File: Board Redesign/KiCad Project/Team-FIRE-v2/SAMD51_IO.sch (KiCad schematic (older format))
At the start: 20 parts, among them SW1 RESET, U5 SAMD51, U6 AT25DF041x-UxN-x, Y1 32.768kHz

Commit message: Fixed some stuff (woops)
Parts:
- R15: footprint Resistor_SMD:R_0603_1608Metric -> (none); Link https://www.mouser.com/ProductDetail/Vishay-Beyschlag/MCT06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 -> (none); MPN MCT06030E1002BP100 -> (none); Manufacturer Vishay -> (none); Supplier Mouser -> (none); Supplier PN 594-MCT06030E1002BP1 -> (none); Tolerance 0.1% -> (none); Type Thin Film Resistor -> (none); Voltage Rating 75 V -> (none)
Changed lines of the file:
@@
 Comment4 ""
 $EndDescr
+Text GLabel 1260 3190 0    50   Input ~ 0
+USB_D-
+Text GLabel 1260 3290 0    50   Input ~ 0
+USB_D+
+Text GLabel 1260 2790 0    50   Input ~ 0
+SDA
+Text GLabel 1260 2890 0    50   Input ~ 0
+SCL
 $Comp
 L Team-FIRE:SAMD51 U?
@@
 	1    0    0    -1
 $EndComp
+Text GLabel 1260 3490 0    50   Input ~ 0
+SWCLK
+Text GLabel 1260 3590 0    50   Input ~ 0
+SWDIO
 Text GLabel 3980 1130 0    50   Input ~ 0
 RX_LED
+Text GLabel 1260 3390 0    50   Input ~ 0
+TX_LED
 Text GLabel 6740 3010 0    50   Input ~ 0
 SWO
@@
 Text Notes 6190 4060 0    50   ~ 10
 SAMD51 Power decoupling capacitors
-Text GLabel 3050 4800 2    50   Input ~ 0
+$Comp
+L Memory_Flash:AT25DF041x-UxN-x U?
+U 1 1 5F15C396
+P 2620 4970
+AR Path="/5E4F8378/5EA71818/5F15C396" Ref="U?"  Part="1"
+AR Path="/5E4F8378/5ED4DEFC/5ED7D75E/5F15C396" Ref="U?"  Part="1"
+AR Path="/5E4F8378/5ED4DEFC/5F15C396" Ref="U6"  Part="1"
+F 0 "U6" H 2770 4550 50  0000 L CNN
+F 1 "AT25DF041x-UxN-x" H 2770 4450 50  0000 L CNN
+F 2 "Package_CSP:WLCSP-8_1.58x1.63x0.35mm_Layout3x5_P0.35x0.4mm_Ball0.25mm_Pad0.25mm_NSMD" H 2420 4370 50  0001 C CNN
+F 3 "http://www.adestotech.com/wp-content/uploads/DS-AT25DF041B_040.pdf" H 2620 5670 50  0001 C CNN
+	1    2620 4970
+	1    0    0    -1
+$EndComp
+Text GLabel 3220 4770 2    50   Input ~ 0
 FLASH_MISO
+Text GLabel 2020 4870 0    50   Input ~ 0
+FLASH_SCK
+Text GLabel 2020 4770 0    50   Input ~ 0
+FLASH_MOSI
+Wire Wire Line
+	2620 5490 2620 5470
 $Comp
 L power:+3.3V #PWR?
 U 1 1 5F15C3A7
-P 2350 4300
+P 2620 4380
 AR Path="/5E4F8378/5EA71818/5F15C3A7" Ref="#PWR?"  Part="1"
 AR Path="/5E4F8378/5ED4DEFC/5ED7D75E/5F15C3A7" Ref="#PWR?"  Part="1"
 AR Path="/5E4F8378/5ED4DEFC/5F15C3A7" Ref="#PWR0138"  Part="1"
-F 0 "#PWR0138" H 2350 4150 50  0001 C CNN
-F 1 "+3.3V" H 2365 4473 50  0000 C CNN
-F 2 "" H 2350 4300 50  0001 C CNN
-F 3 "" H 2350 4300 50  0001 C CNN
-	1    2350 4300
-	1    0    0    -1
-$EndComp
+F 0 "#PWR0138" H 2620 4230 50  0001 C CNN
+F 1 "+3.3V" H 2635 4553 50  0000 C CNN
+F 2 "" H 2620 4380 50  0001 C CNN
+F 3 "" H 2620 4380 50  0001 C CNN
+	1    2620 4380
+	1    0    0    -1
+$EndComp
+Wire Wire Line
+	2620 4380 2620 4460
+Wire Wire Line
+	2020 4970 1920 4970
+Wire Wire Line
+	2020 5070 1920 5070
+Wire Wire Line
+	1920 5070 1920 4970
+Connection ~ 1920 4970
+Wire Wire Line
+	1920 5070 1670 5070
+Connection ~ 1920 5070
+Connection ~ 2620 4460
+Wire Wire Line
+	2620 4460 2620 4470
+Wire Wire Line
+	1270 4820 1270 4970
+Wire Wire Line
+	1270 4520 1270 4460
+Wire Wire Line
+	2020 5170 1920 5170
+Wire Wire Line
+	1920 5170 1920 5070
+Wire Wire Line
+	1270 4460 2620 4460
+Wire Wire Line
+	1270 4970 1920 4970
+Text Notes 970  4020 0    50   ~ 10
+Flash Memory
 $Comp
 L Device:Crystal Y?
@@
 Wire Notes Line
 	3990 4080 5940 4080
+Wire Notes Line
+	990  4050 3750 4050
+Wire Notes Line
+	3750 4050 3750 5730
+Wire Notes Line
+	3750 5730 990  5730
+Wire Notes Line
+	990  5730 990  4060
 Connection ~ 8620 4640
 Wire Wire Line
@@
 	8310 4510 8310 4640
 Connection ~ 8620 4510
+Text GLabel 1260 1590 0    50   Input ~ 0
+FLASH_MOSI
+Text GLabel 1260 1790 0    50   Input ~ 0
+FLASH_CS
+Text GLabel 1260 1890 0    50   Input ~ 0
+FLASH_MISO
+Text GLabel 1260 1690 0    50   Input ~ 0
+FLASH_SCK
+Text GLabel 1260 2290 0    50   Input ~ 0
+IO-RTS
+Text GLabel 1260 1990 0    50   Input ~ 0
+IO-CTS
+Text GLabel 1260 2190 0    50   Input ~ 0
+IO-DSR
+Text GLabel 1260 2390 0    50   Input ~ 0
+IO-DCD
 Text GLabel 3980 2630 0    50   Input ~ 0
 IO-RI
+Text GLabel 1260 2590 0    50   Input ~ 0
+IO-TX
+Text GLabel 1260 2690 0    50   Input ~ 0
+IO-RX
 Text GLabel 3980 1830 0    50   Input ~ 0
 IO-DTR
@@
 	1    0    0    -1
 $EndComp
+$Comp
+L Device:R R?
+U 1 1 5F15C3AE
+P 1270 4670
+AR Path="/5E4F8378/5EA71818/5F15C3AE" Ref="R?"  Part="1"
+AR Path="/5E4F8378/5ED4DEFC/5ED7D75E/5F15C3AE" Ref="R?"  Part="1"
+AR Path="/5E4F8378/5ED4DEFC/5F15C3AE" Ref="R15"  Part="1"
+F 0 "R15" H 1340 4716 50  0000 L CNN
+F 1 "10k" H 1340 4625 50  0000 L CNN
+F 2 "" V 1200 4670 50  0001 C CNN
+F 3 "~" H 1270 4670 50  0001 C CNN
+	1    1270 4670
+	1    0    0    -1
+$EndComp
 NoConn ~ 1260 990
 NoConn ~ 1260 1090
@@
 Text GLabel 1850 6470 2    50   Input ~ 0
 XIN32
-Wire Wire Line
-	1750 4800 1650 4800
-Text GLabel 1550 5100 0    50   Input ~ 0
+$Comp
+L power:GND #PWR?
+U 1 1 5F15C3A0
+P 2620 5490
+AR Path="/5E4F8378/5EA71818/5F15C3A0" Ref="#PWR?"  Part="1"
+AR Path="/5E4F8378/5ED4DEFC/5ED7D75E/5F15C3A0" Ref="#PWR?"  Part="1"
+AR Path="/5E4F8378/5ED4DEFC/5F15C3A0" Ref="#PWR0137"  Part="1"
+F 0 "#PWR0137" H 2620 5240 50  0001 C CNN
+F 1 "GND" H 2625 5317 50  0000 C CNN
+F 2 "" H 2620 5490 50  0001 C CNN
+F 3 "" H 2620 5490 50  0001 C CNN
+	1    2620 5490
+	1    0    0    -1
+$EndComp
+Text GLabel 1670 5070 0    50   Input ~ 0
 FLASH_CS
-Wire Wire Line
-	1750 5100 1650 5100
-Wire Wire Line
-	1750 5200 1650 5200
-Wire Wire Line
-	1650 5000 1750 5000
-Wire Wire Line
-	1650 5000 1650 5100
-Connection ~ 1650 5100
-Wire Wire Line
-	1650 5100 1550 5100
-Wire Wire Line
-	1650 5100 1650 5200
-Wire Wire Line
-	2350 4300 2350 4400
-Wire Wire Line
-	2950 4800 3050 4800
-$Comp
-L power:GND #PWR?
-U 1 1 5EBDC8BA
-P 2350 5500
-AR Path="/5E4F8378/5EA71818/5EBDC8BA" Ref="#PWR?"  Part="1"
-AR Path="/5E4F8378/5ED4DEFC/5ED7D75E/5EBDC8BA" Ref="#PWR?"  Part="1"
-AR Path="/5E4F8378/5ED4DEFC/5EBDC8BA" Ref="#PWR013"  Part="1"
-F 0 "#PWR013" H 2350 5250 50  0001 C CNN
-F 1 "GND" H 2355 5327 50  0000 C CNN
-F 2 "" H 2350 5500 50  0001 C CNN
-F 3 "" H 2350 5500 50  0001 C CNN
-	1    2350 5500
-	1    0    0    -1
-$EndComp
-Wire Wire Line
-	1650 4900 1750 4900
-Text GLabel 1650 4900 0    50   Input ~ 0
-FLASH_SCK
-Text GLabel 1650 4800 0    50   Input ~ 0
-FLASH_MOSI
-$Comp
-L Device:R R?
-U 1 1 5EBDEFB3
-P 1050 4750
-AR Path="/5E4F8378/5EBDEFB3" Ref="R?"  Part="1"
-AR Path="/5E4F8378/5ED4DEFC/5EBDEFB3" Ref="R15"  Part="1"
-F 0 "R15" H 800 4800 50  0000 L CNN
-F 1 "10k" H 800 4700 50  0000 L CNN
-F 2 "Resistor_SMD:R_0603_1608Metric" V 980 4750 50  0001 C CNN
-F 3 "https://www.mouser.com/datasheet/2/427/mcx0x0xpre-1762843.pdf" H 1050 4750 50  0001 C CNN
-F 4 "MCT06030E1002BP100" H 1050 4750 50  0001 C CNN "MPN"
-F 5 "Vishay" H 1050 4750 50  0001 C CNN "Manufacturer"
-F 6 "Mouser" H 1050 4750 50  0001 C CNN "Supplier"
-F 7 "594-MCT06030E1002BP1" H 1050 4750 50  0001 C CNN "Supplier PN"
-F 8 "https://www.mouser.com/ProductDetail/Vishay-Beyschlag/MCT06030E1002BP100?qs=sGAEpiMZZMtlubZbdhIBIHIEm3drdiPa32EPxwxqfD0%3D" H 1050 4750 50  0001 C CNN "Link"
-F 9 "Thin Film Resistor" H 1050 4750 50  0001 C CNN "Type"
-F 10 "0.1%" H 1050 4750 50  0001 C CNN "Tolerance"
-F 11 "75 V" H 1050 4750 50  0001 C CNN "Voltage Rating"
-	1    1050 4750
-	1    0    0    -1
-$EndComp
-Wire Wire Line
-	1650 5000 1050 5000
-Wire Wire Line
-	1050 5000 1050 4900
-Connection ~ 1650 5000
-Wire Wire Line
-	1050 4600 1050 4400
-Wire Wire Line
-	1050 4400 2350 4400
-Connection ~ 2350 4400
-Wire Wire Line
-	2350 4400 2350 4500
-Wire Notes Line
-	700  4050 3650 4050
-Wire Notes Line
-	3650 4050 3650 5800
-Wire Notes Line
-	3650 5800 700  5800
-Wire Notes Line
-	700  5800 700  4050
-Text Notes 700  4050 0    79   ~ 16
-Flash Memory
-$Comp
-L Memory_Flash:AT25DF041x-UxN-x U6
-U 1 1 5EBC3761
-P 2350 5000
-F 0 "U6" H 2500 5450 50  0000 L CNN
-F 1 "AT25DF041x-UxN-x" H 2994 4955 50  0001 L CNN
-F 2 "Package_CSP:WLCSP-8_1.58x1.63x0.35mm_Layout3x5_P0.35x0.4mm_Ball0.25mm_Pad0.25mm_NSMD" H 2150 4400 50  0001 C CNN
-F 3 "http://www.adestotech.com/wp-content/uploads/DS-AT25DF041B_040.pdf" H 2350 5700 50  0001 C CNN
-	1    2350 5000
-	1    0    0    -1
-$EndComp
-Text GLabel 1260 2740 0    50   Input ~ 0
-USB_D-
-Text GLabel 1260 2840 0    50   Input ~ 0
-USB_D+
-Text GLabel 1260 2340 0    50   Input ~ 0
-SDA
-Text GLabel 1260 2440 0    50   Input ~ 0
-SCL
-Text GLabel 1260 3040 0    50   Input ~ 0
-SWCLK
-Text GLabel 1260 3140 0    50   Input ~ 0
-SWDIO
-Text GLabel 1260 2940 0    50   Input ~ 0
-TX_LED
-Text GLabel 1260 1140 0    50   Input ~ 0
-FLASH_MOSI
-Text GLabel 1260 1340 0    50   Input ~ 0
-FLASH_CS
-Text GLabel 1260 1440 0    50   Input ~ 0
-FLASH_MISO
-Text GLabel 1260 1240 0    50   Input ~ 0
-FLASH_SCK
-Text GLabel 1260 1840 0    50   Input ~ 0
-IO-RTS
-Text GLabel 1260 1540 0    50   Input ~ 0
-IO-CTS
-Text GLabel 1260 1740 0    50   Input ~ 0
-IO-DSR
-Text GLabel 1260 1940 0    50   Input ~ 0
-IO-DCD
-Text GLabel 1260 2140 0    50   Input ~ 0
-IO-TX
-Text GLabel 1260 2240 0    50   Input ~ 0
-IO-RX
 $EndSCHEMATC

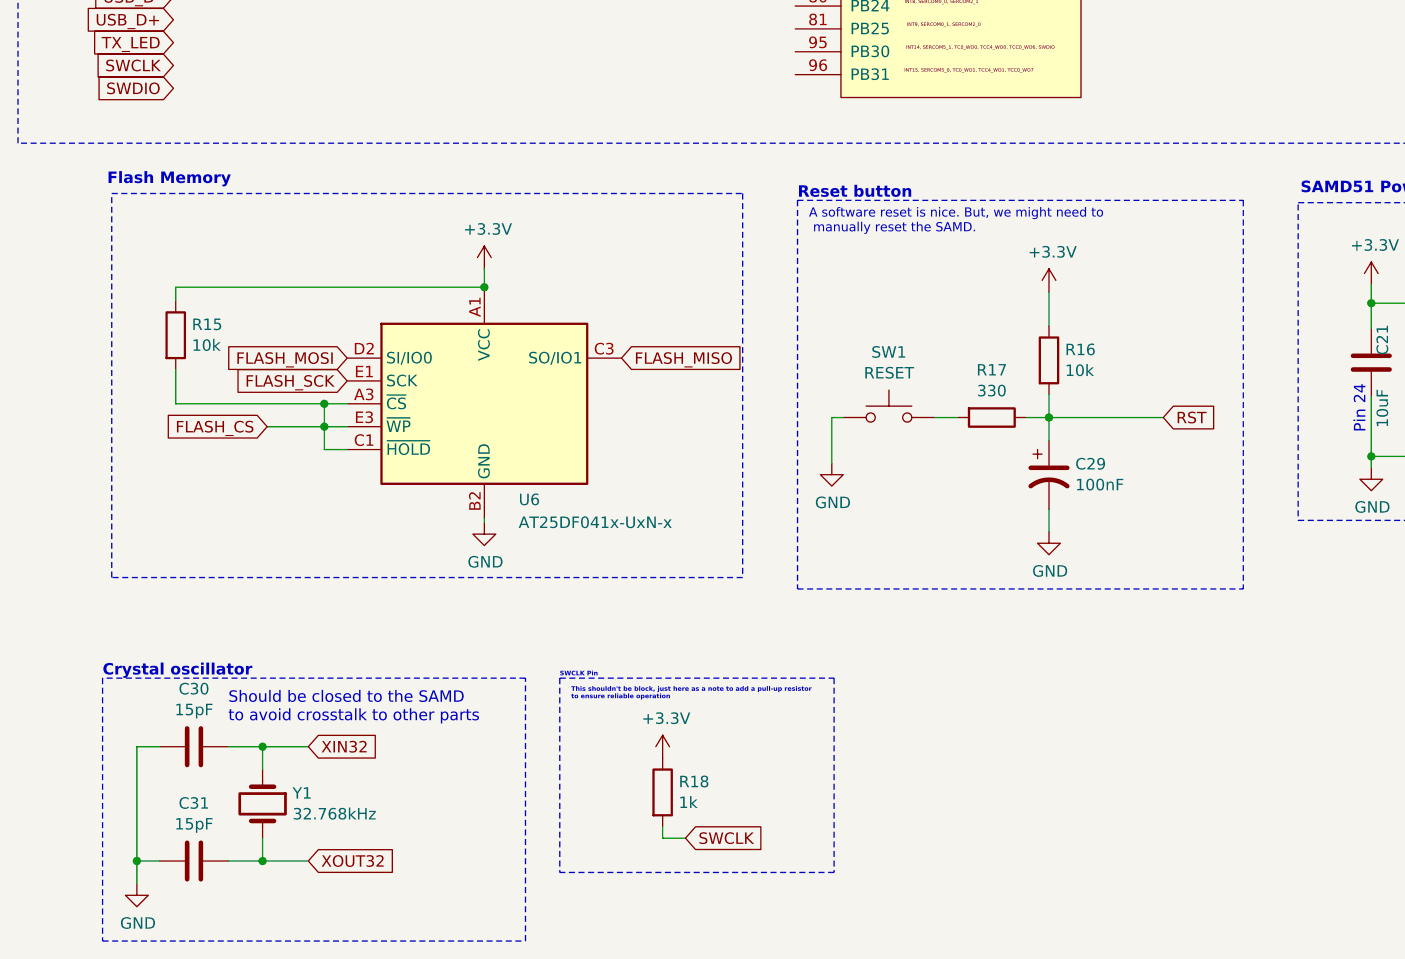
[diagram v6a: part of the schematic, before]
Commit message: Fixed alignment(s), added component details
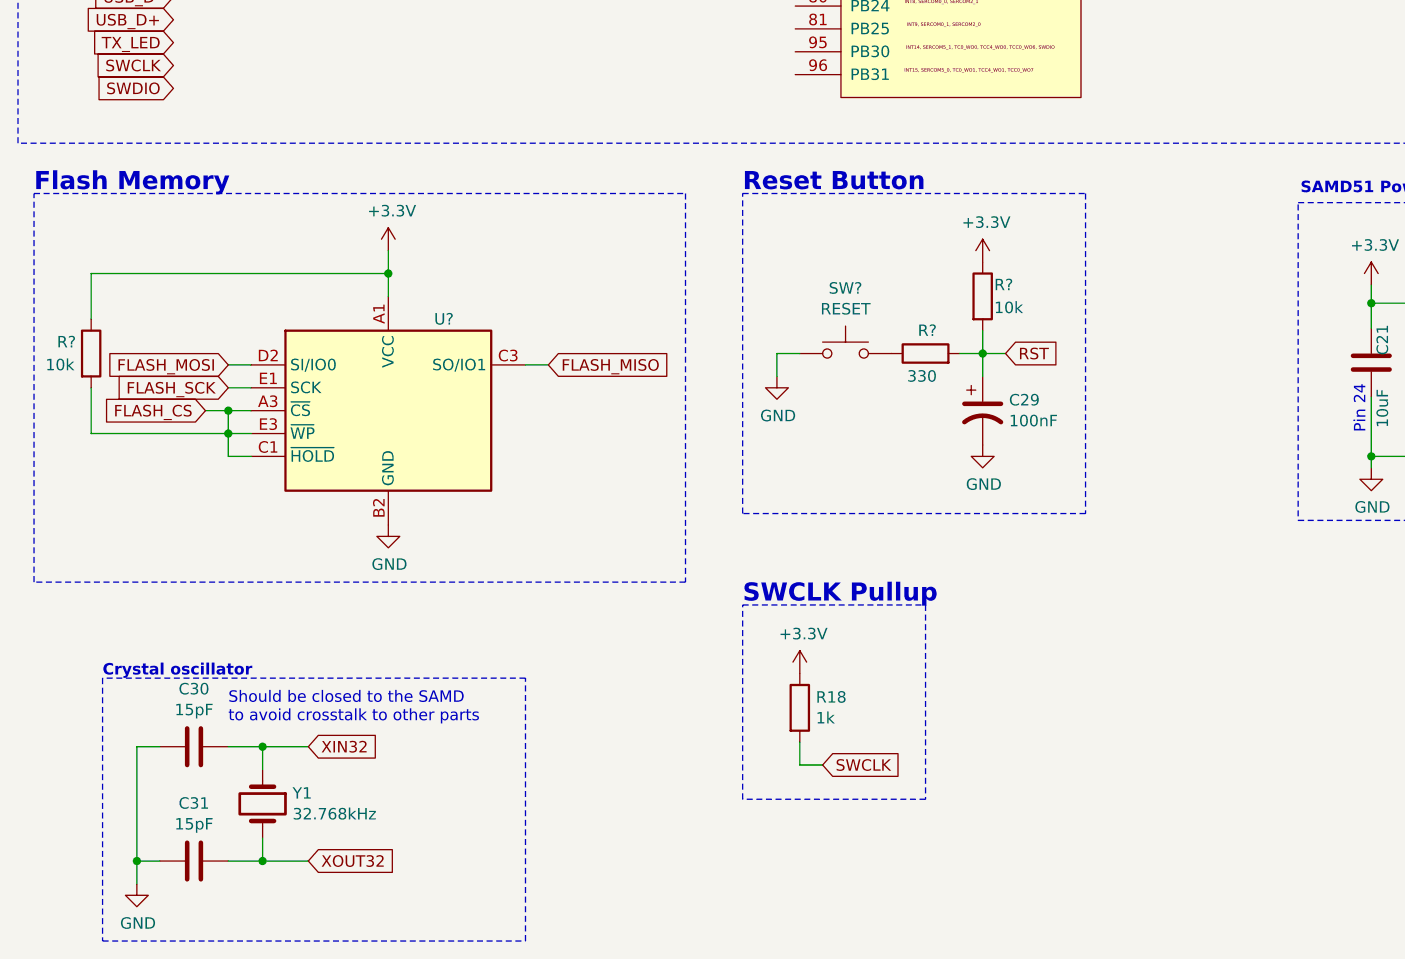
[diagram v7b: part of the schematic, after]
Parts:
- removed R15: 10k, symbol Device:R
- removed R16: 10k, Resistor_SMD:R_0603_1608Metric, symbol Device:R
- removed R17: 330, Resistor_SMD:R_0603_1608Metric, symbol Device:R
- removed SW1: RESET, Button_Switch_SMD:SW_SPST_EVQQ2, symbol Switch:SW_Push
- removed U6: AT25DF041x-UxN-x, Package_CSP:WLCSP-8_1.58x1.63x0.35mm_Layout3x5_P0.35x0.4mm_Ball0.25mm_Pad0.25mm_NSMD, symbol Memory_Flash:AT25DF041x-UxN-x
- added R? (x2): 10k, Resistor_SMD:R_0603_1608Metric, symbol Device:R
- added R?: 330, Resistor_SMD:R_0603_1608Metric, symbol Device:R
- added SW?: RESET, Button_Switch_SMD:SW_SPST_EVQQ2, symbol Switch:SW_Push
- added U?: AT25DF041x-UxN-x, Package_CSP:WLCSP-8_1.58x1.63x0.35mm_Layout3x5_P0.35x0.4mm_Ball0.25mm_Pad0.25mm_NSMD, symbol Memory_Flash:AT25DF041x-UxN-x
- R18: Link (none) -> https://www.mouser.com/ProductDetail/Vishay-Beyschlag/MCT06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; MPN (none) -> MCT0603MD1001BP500; Manufacturer (none) -> Vishay; Supplier (none) -> Mouser; Supplier PN (none) -> 594-MCT0603MD1001BP5; Tolerance (none) -> 0.1%; Type (none) -> Thin Film Resistor; Voltage Rating (none) -> 75 V
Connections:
- net +3V3: now also R?.1, R?.1, U?.A1 (VCC)
- net FLASH_CS: now also R?.2, U?.A3 (~CS), U?.C1 (~HOLD~), U?.E3 (~WP~)
- net FLASH_MISO: now also U?.C3 (SO/IO1)
- net FLASH_MOSI: now also U?.D2 (SI/IO0)
- net FLASH_SCK: now also U?.E1 (SCK)
- net GND: now also SW?.1, U?.B2 (GND)
- net RST: now also R?.2, R?.2
- new net: R?.1, SW?.2
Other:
- note added: "Flash Memory\n"
- note added: "Reset Button"
- note added: "SWCLK Pullup\n"
- note removed: "A software reset is nice. But, we might need to\n manually reset the SAMD."
- note removed: "Flash Memory"
- note removed: "Reset button"
- note removed: "SWCLK Pin"
- note removed: "This shouldn't be block, just here as a note to add a pull-up resistor\nto ensure reliable operation"
- moved on the sheet: C29, R18
